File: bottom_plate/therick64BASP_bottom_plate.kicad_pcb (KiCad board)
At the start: 2 copper layers, 313.9 x 76 mm, 80 parts, among them U1 HOLE, U10 HOLE, U11 HOLE, U12 HOLE, U13 HOLE, U14 HOLE, U15 HOLE, U16 HOLE, U17 HOLE, U18 HOLE, U19 HOLE, U2 HOLE, U20 HOLE, U21 HOLE, U22 HOLE, U23 HOLE, U24 HOLE, U25 HOLE, U26 HOLE, U27 HOLE, U28 HOLE, U29 HOLE, U3 HOLE, U30 HOLE, U31 HOLE, U32 HOLE, U33 HOLE, U34 HOLE, U35 HOLE, U36 HOLE, U37 HOLE, U38 HOLE, U39 HOLE, U4 HOLE, U40 HOLE, U41 HOLE, U42 HOLE, U43 HOLE, U44 HOLE, U45 HOLE, U46 HOLE, U47 HOLE, U48 HOLE, U49 HOLE, U5 HOLE, U50 HOLE, U51 HOLE, U52 HOLE, U53 HOLE, U54 HOLE, U55 HOLE, U56 HOLE, U57 HOLE, U58 HOLE, U59 HOLE, U6 HOLE, U60 HOLE, U61 HOLE, U62 HOLE, U63 HOLE, U64 HOLE, U65 HOLE, U66 HOLE, U67 HOLE, U68 HOLE, U69 HOLE, U7 HOLE, U70 HOLE, U8 HOLE, U9 HOLE

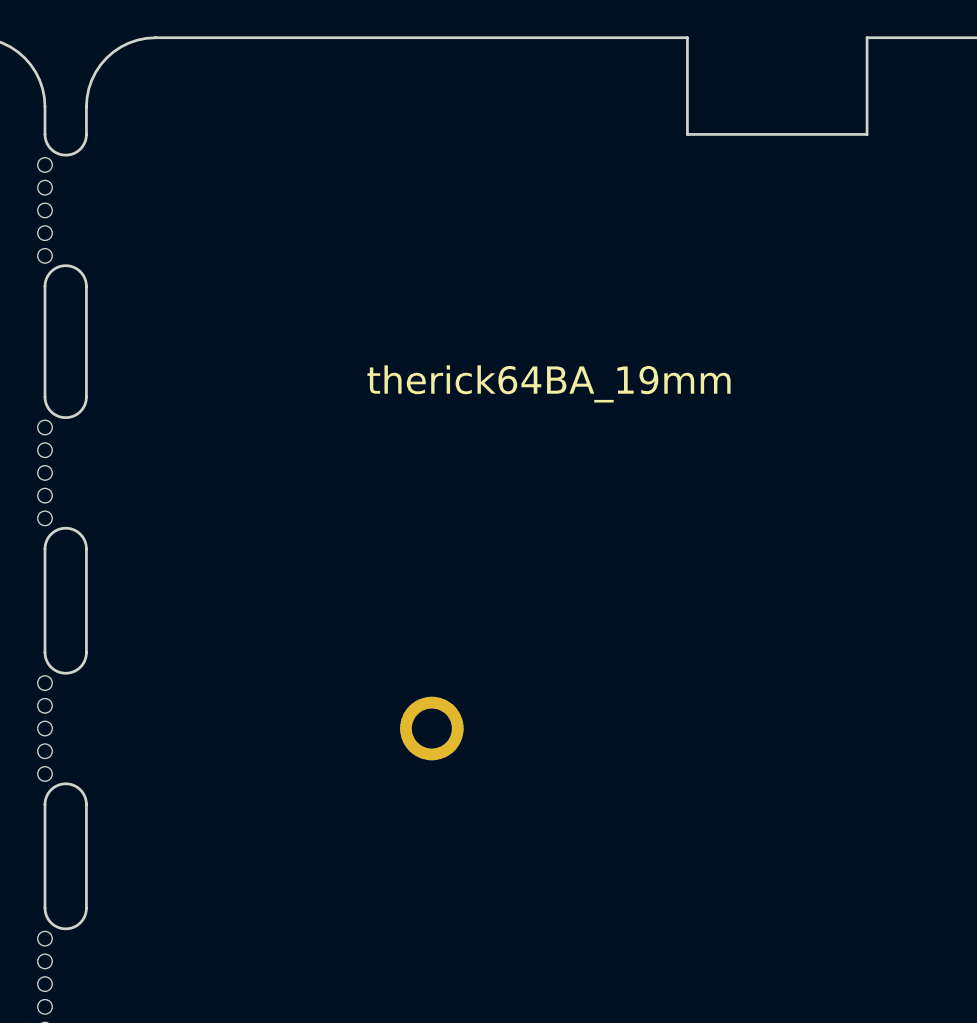
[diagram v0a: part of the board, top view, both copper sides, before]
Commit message: Changed pins to make routing cleaner
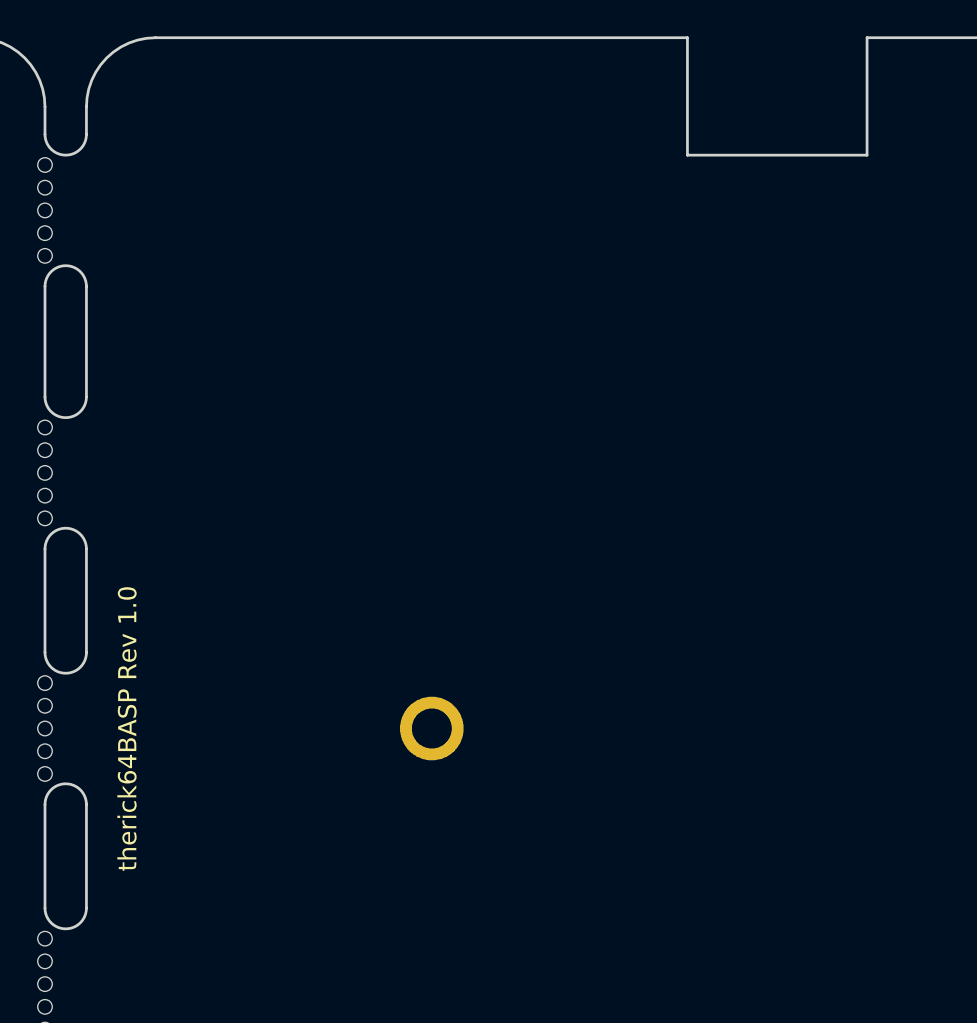
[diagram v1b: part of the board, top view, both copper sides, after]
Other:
- outline, holes or cut-outs redrawn
- board text added: "therick64BASP Rev 1.0"
- board text removed: "therick"
- board text removed: "therick64BA_19mm"
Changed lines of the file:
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@@
   (general
     (thickness 1.6)
-    (drawings 69)
+    (drawings 68)
     (tracks 0)
     (zones 0)
@@
     (solder_mask_min_width 0.25)
     (aux_axis_origin 160.3375 73.025)
-    (visible_elements 7FFFFFFF)
+    (visible_elements 7FFFEFFF)
     (pcbplotparams
       (layerselection 0x010fc_ffffffff)
@@
   )
   (gr_line (start 60.04 112.86) (end 60.04 44.46) (layer Edge.Cuts) (width 0.15))
-  (gr_text therick64BA_19mm (at 161.320286 59.548) (layer F.SilkS)
-    (effects (font (size 1.5 1.5) (thickness 0.2)) (justify left))
+  (gr_text "therick64BASP Rev 1.0" (at 148.19961 78.659793 90) (layer F.SilkS)
+    (effects (font (size 1 1) (thickness 0.15)))
   )
   (gr_arc (start 144.78 111.34) (end 145.92 111.34) (angle -180) (layer Edge.Cuts) (width 0.15))
@@
   (gr_arc (start 139.84 44.46) (end 143.64 44.46) (angle -90) (layer Edge.Cuts) (width 0.15))
   (gr_arc (start 139.84 112.86) (end 139.84 116.66) (angle -90) (layer Edge.Cuts) (width 0.15))
-  (gr_line (start 188.86 45.98) (end 188.86 40.66) (layer Edge.Cuts) (width 0.15))
-  (gr_line (start 178.98 45.98) (end 188.86 45.98) (layer Edge.Cuts) (width 0.15))
-  (gr_line (start 178.98 40.66) (end 178.98 45.98) (layer Edge.Cuts) (width 0.15))
+  (gr_line (start 188.86 47.119876) (end 188.86 40.66) (layer Edge.Cuts) (width 0.15))
+  (gr_line (start 178.979529 47.119876) (end 188.859529 47.119876) (layer Edge.Cuts) (width 0.15))
+  (gr_line (start 178.98 40.66) (end 178.98 47.119876) (layer Edge.Cuts) (width 0.15))
   (gr_line (start 149.72 116.66) (end 370.12 116.66) (layer Edge.Cuts) (width 0.15))
   (gr_line (start 149.72 40.66) (end 178.98 40.66) (layer Edge.Cuts) (width 0.15))
@@
   (gr_line (start 201.16 59.675) (end 204.335 59.675) (layer Dwgs.User) (width 0.15))
   (gr_line (start 202.7475 61.2625) (end 202.7475 57.29375) (layer Dwgs.User) (width 0.15))
-  (gr_text therick (at 317.68 115.174) (layer B.SilkS)
-    (effects (font (size 1.5 1.5) (thickness 0.2)) (justify left mirror))
-  )
 )

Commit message: Remapped ISP Flash, added mounting holes
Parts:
- added H11: MountingHole, random-keyboard-parts:Generic-Mounthole, F.Cu at (164.9, 97.7)
- added H12: MountingHole, random-keyboard-parts:Generic-Mounthole, F.Cu at (164.9, 59.7)
- added H13: MountingHole, random-keyboard-parts:Generic-Mounthole, F.Cu at (221.9, 59.7)
- added H14: MountingHole, random-keyboard-parts:Generic-Mounthole, F.Cu at (221.9, 97.7)
- added H15: MountingHole, random-keyboard-parts:Generic-Mounthole, F.Cu at (297.9, 59.7)
- added H16: MountingHole, random-keyboard-parts:Generic-Mounthole, F.Cu at (297.9, 97.7)
- added H17: MountingHole, random-keyboard-parts:Generic-Mounthole, F.Cu at (354.9, 59.7)
- added H18: MountingHole, random-keyboard-parts:Generic-Mounthole, F.Cu at (354.9, 97.7)
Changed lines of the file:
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@@
     (tracks 0)
     (zones 0)
-    (modules 80)
+    (modules 88)
     (nets 1)
   )
@@
     (uvia_drill 0.2)
   )
+  (module random-keyboard-parts:Generic-Mounthole (layer F.Cu)
+    (at 354.92 97.66)
+    (attr virtual)
+    (fp_text reference H18 (at 0 2) (layer Dwgs.User)
+      (effects (font (size 1 1) (thickness 0.15)))
+    )
+    (fp_text value MountingHole (at 0 -2) (layer Dwgs.User)
+      (effects (font (size 1 1) (thickness 0.15)))
+    )
+    (pad 1 thru_hole circle (at 0 0) (size 3.5 3.5) (drill 2.2) (layers *.Cu *.Mask))
+  )
+  (module random-keyboard-parts:Generic-Mounthole (layer F.Cu)
+    (at 354.92 59.66)
+    (attr virtual)
+    (fp_text reference H17 (at 0 2) (layer Dwgs.User)
+      (effects (font (size 1 1) (thickness 0.15)))
+    )
+    (fp_text value MountingHole (at 0 -2) (layer Dwgs.User)
+      (effects (font (size 1 1) (thickness 0.15)))
+    )
+    (pad 1 thru_hole circle (at 0 0) (size 3.5 3.5) (drill 2.2) (layers *.Cu *.Mask))
+  )
+  (module random-keyboard-parts:Generic-Mounthole (layer F.Cu)
+    (at 297.92 97.66)
+    (attr virtual)
+    (fp_text reference H16 (at 0 2) (layer Dwgs.User)
+      (effects (font (size 1 1) (thickness 0.15)))
+    )
+    (fp_text value MountingHole (at 0 -2) (layer Dwgs.User)
+      (effects (font (size 1 1) (thickness 0.15)))
+    )
+    (pad 1 thru_hole circle (at 0 0) (size 3.5 3.5) (drill 2.2) (layers *.Cu *.Mask))
+  )
+  (module random-keyboard-parts:Generic-Mounthole (layer F.Cu)
+    (at 297.92 59.66)
+    (attr virtual)
+    (fp_text reference H15 (at 0 2) (layer Dwgs.User)
+      (effects (font (size 1 1) (thickness 0.15)))
+    )
+    (fp_text value MountingHole (at 0 -2) (layer Dwgs.User)
+      (effects (font (size 1 1) (thickness 0.15)))
+    )
+    (pad 1 thru_hole circle (at 0 0) (size 3.5 3.5) (drill 2.2) (layers *.Cu *.Mask))
+  )
+  (module random-keyboard-parts:Generic-Mounthole (layer F.Cu)
+    (at 221.92 97.66)
+    (attr virtual)
+    (fp_text reference H14 (at 0 2) (layer Dwgs.User)
+      (effects (font (size 1 1) (thickness 0.15)))
+    )
+    (fp_text value MountingHole (at 0 -2) (layer Dwgs.User)
+      (effects (font (size 1 1) (thickness 0.15)))
+    )
+    (pad 1 thru_hole circle (at 0 0) (size 3.5 3.5) (drill 2.2) (layers *.Cu *.Mask))
+  )
+  (module random-keyboard-parts:Generic-Mounthole (layer F.Cu)
+    (at 221.92 59.66)
+    (attr virtual)
+    (fp_text reference H13 (at 0 2) (layer Dwgs.User)
+      (effects (font (size 1 1) (thickness 0.15)))
+    )
+    (fp_text value MountingHole (at 0 -2) (layer Dwgs.User)
+      (effects (font (size 1 1) (thickness 0.15)))
+    )
+    (pad 1 thru_hole circle (at 0 0) (size 3.5 3.5) (drill 2.2) (layers *.Cu *.Mask))
+  )
+  (module random-keyboard-parts:Generic-Mounthole (layer F.Cu)
+    (at 164.92 59.66)
+    (attr virtual)
+    (fp_text reference H12 (at 0 2) (layer Dwgs.User)
+      (effects (font (size 1 1) (thickness 0.15)))
+    )
+    (fp_text value MountingHole (at 0 -2) (layer Dwgs.User)
+      (effects (font (size 1 1) (thickness 0.15)))
+    )
+    (pad 1 thru_hole circle (at 0 0) (size 3.5 3.5) (drill 2.2) (layers *.Cu *.Mask))
+  )
+  (module random-keyboard-parts:Generic-Mounthole (layer F.Cu)
+    (at 164.92 97.66)
+    (attr virtual)
+    (fp_text reference H11 (at 0 2) (layer Dwgs.User)
+      (effects (font (size 1 1) (thickness 0.15)))
+    )
+    (fp_text value MountingHole (at 0 -2) (layer Dwgs.User)
+      (effects (font (size 1 1) (thickness 0.15)))
+    )
+    (pad 1 thru_hole circle (at 0 0) (size 3.5 3.5) (drill 2.2) (layers *.Cu *.Mask))
+  )
   (module Keeb_footprints:MX100_outline (layer F.Cu)

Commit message: Add reset hole
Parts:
- added H19: MountingHole, random-keyboard-parts:Generic-Mounthole, F.Cu at (202.9, 51.7)
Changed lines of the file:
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@@
     (tracks 0)
     (zones 0)
-    (modules 88)
+    (modules 89)
     (nets 1)
   )
@@
   )
   (module random-keyboard-parts:Generic-Mounthole (layer F.Cu)
+    (at 202.9073 51.68)
+    (attr virtual)
+    (fp_text reference H19 (at 0 2) (layer Dwgs.User)
+      (effects (font (size 1 1) (thickness 0.15)))
+    )
+    (fp_text value MountingHole (at 0 -2) (layer Dwgs.User)
+      (effects (font (size 1 1) (thickness 0.15)))
+    )
+    (pad 1 thru_hole circle (at 0 0) (size 3.5 3.5) (drill 2.2) (layers *.Cu *.Mask))
+  )
+  (module random-keyboard-parts:Generic-Mounthole (layer F.Cu)
